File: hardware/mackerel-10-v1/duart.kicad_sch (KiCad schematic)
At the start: 2 parts, among them U6 XR68C681, X2 3.6864 MHz

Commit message: Trying to figure out Mackerel-10 components
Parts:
- added J3, J7: DE9_Plug_MountingHoles, Connector_Dsub:DSUB-9_Male_Horizontal_P2.77x2.84mm_EdgePinOffset7.70mm_Housed_MountingHolesOffset9.12mm, symbol Connector:DE9_Plug_MountingHoles
- added J4, J5: Conn_01x06, Connector_PinSocket_2.54mm:PinSocket_1x06_P2.54mm_Horizontal, symbol Connector_Generic:Conn_01x06
- added JP1, JP2: Jumper_2_Open, Connector_PinHeader_2.54mm:PinHeader_1x02_P2.54mm_Vertical, symbol Jumper:Jumper_2_Open
- added U8, U9: MAX3232, Package_DIP:DIP-16_W7.62mm, symbol Interface_UART:MAX3232
- renumbered U6 to U7
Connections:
- net +5V: now also JP1.1 (A), JP2.1 (A)
- net GND: now also J4.1 (Pin_1), J5.1 (Pin_1)
- new net: J5.3 (Pin_3), JP2.2 (B)
- new net: J4.3 (Pin_3), JP1.2 (B)
- new net RXA: J4.4 (Pin_4)
- new net RXB: J5.4 (Pin_4)
- new net TXA: J4.5 (Pin_5)
- new net TXB: J5.5 (Pin_5)
- new net /RTSA: J4.2 (Pin_2)
- new net /RTSB: J5.2 (Pin_2)
- no-connect marks 2 -> 4
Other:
- note added: "UART Headers"

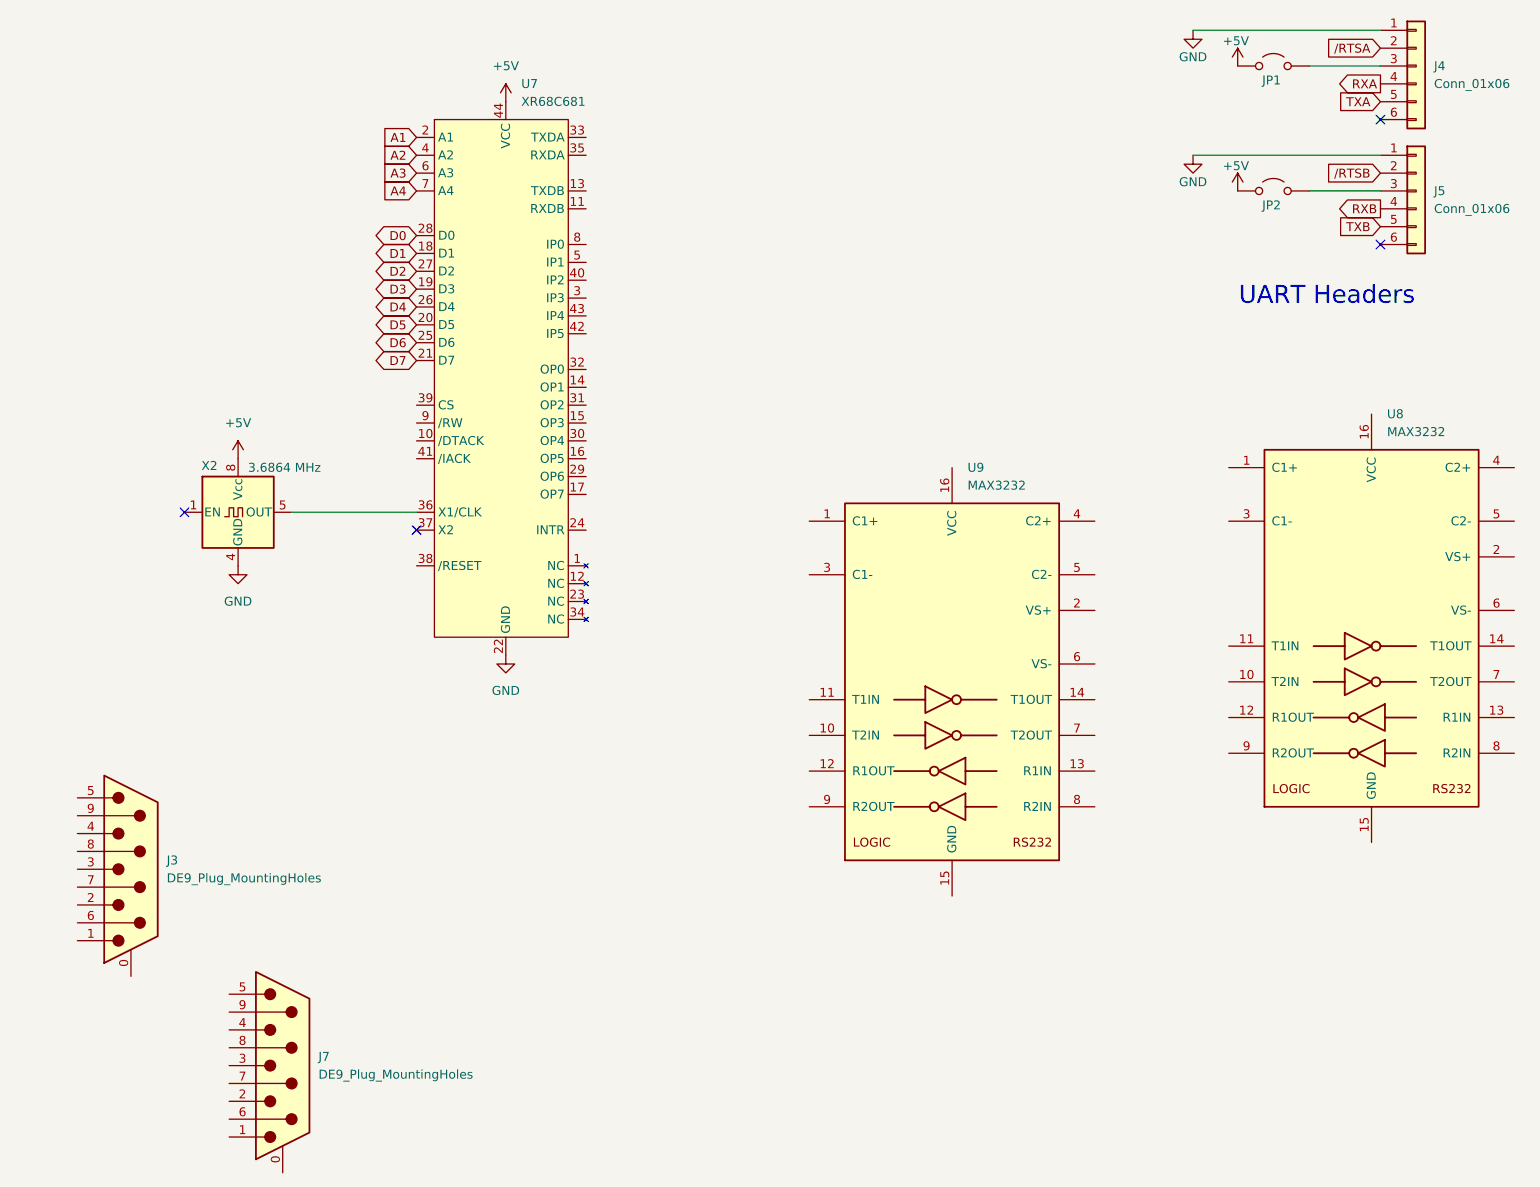
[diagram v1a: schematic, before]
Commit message: More progress on Mackerel-10 schematic and PCB
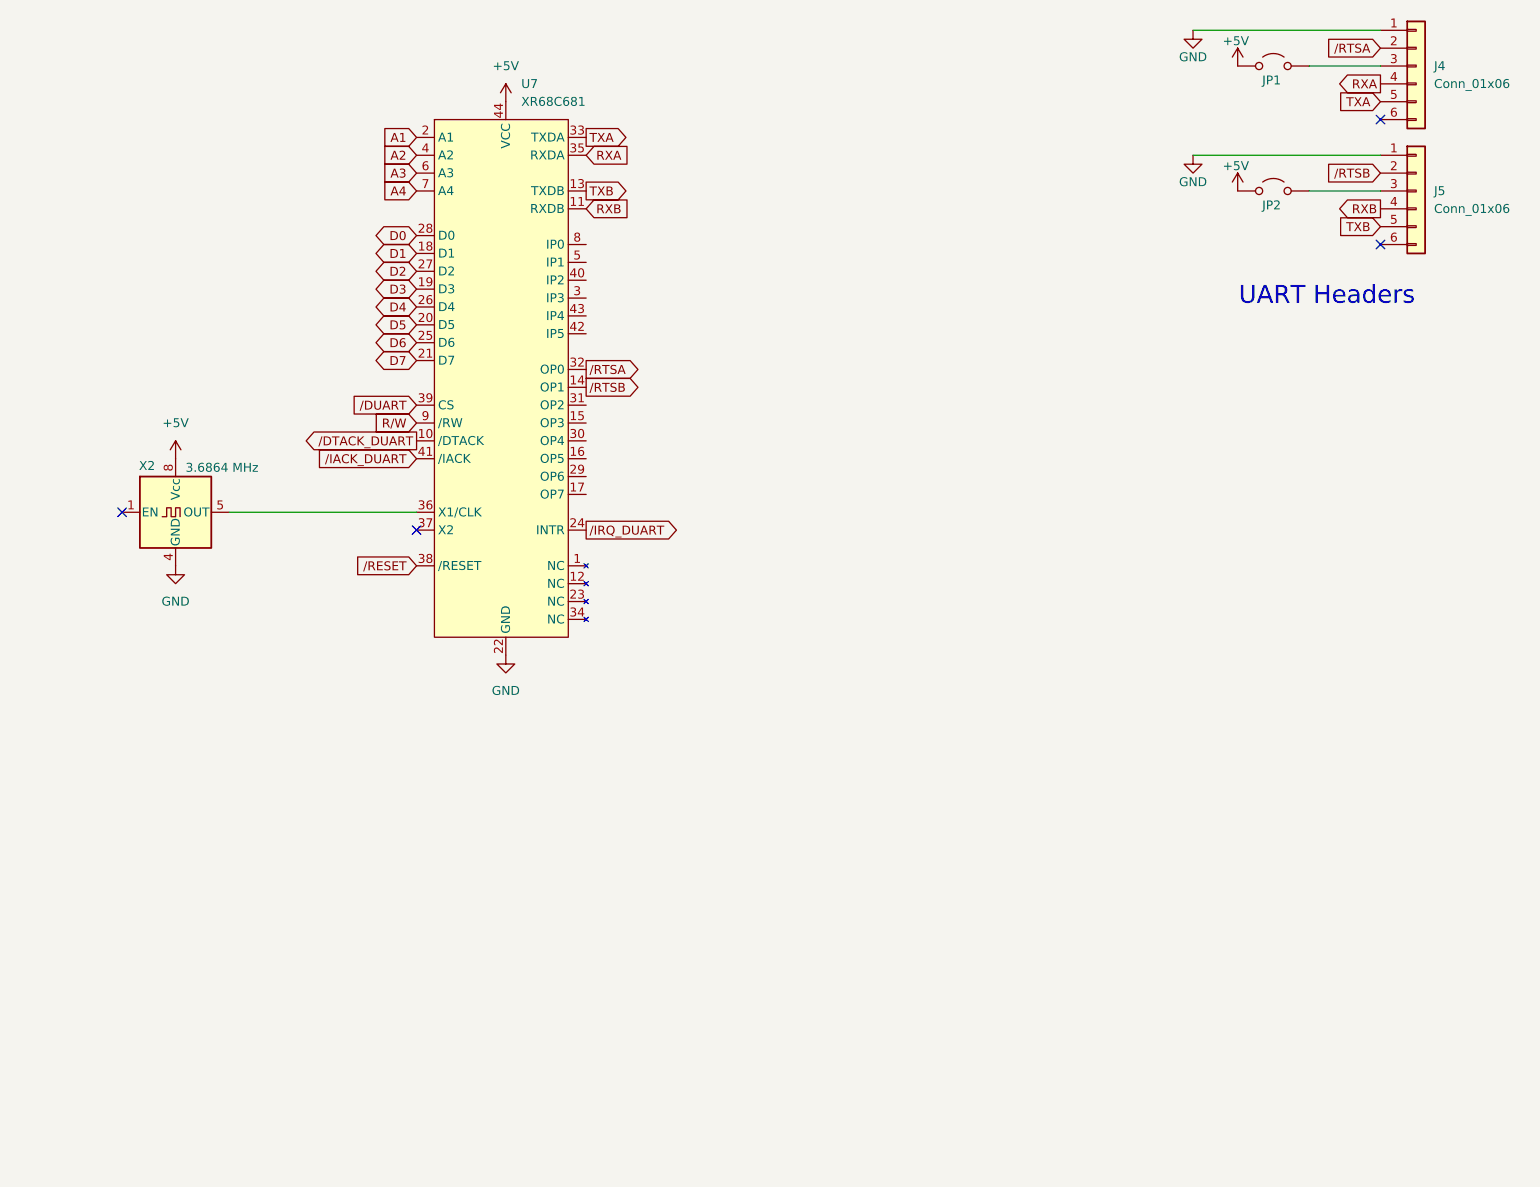
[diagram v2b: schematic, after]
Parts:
- removed J3, J7: DE9_Plug_MountingHoles, Connector_Dsub:DSUB-9_Male_Horizontal_P2.77x2.84mm_EdgePinOffset7.70mm_Housed_MountingHolesOffset9.12mm, symbol Connector:DE9_Plug_MountingHoles
- removed U8, U9: MAX3232, Package_DIP:DIP-16_W7.62mm, symbol Interface_UART:MAX3232
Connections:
- net RXA: now also U7.35 (RXDA)
- net RXB: now also U7.11 (RXDB)
- net TXA: now also U7.33 (TXDA)
- net TXB: now also U7.13 (TXDB)
- net /RTSA: now also U7.32 (OP0)
- net /RTSB: now also U7.14 (OP1)
- net /DTACK_DUART: now reaches U7.10 (/DTACK)
- net /IRQ_DUART: now reaches U7.24 (INTR)
- net /RESET: now reaches U7.38 (/RESET)
- net /DUART: now reaches U7.39 (CS)
- net /IACK_DUART: now reaches U7.41 (/IACK)
- net R/W: now reaches U7.9 (/RW)
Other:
- moved on the sheet: X2

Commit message: Rough layout of simplified Mack-10 prototype
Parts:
- removed JP1, JP2: Jumper_2_Open, Connector_PinHeader_2.54mm:PinHeader_1x02_P2.54mm_Vertical, symbol Jumper:Jumper_2_Open
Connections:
- no-connect marks 4 -> 6

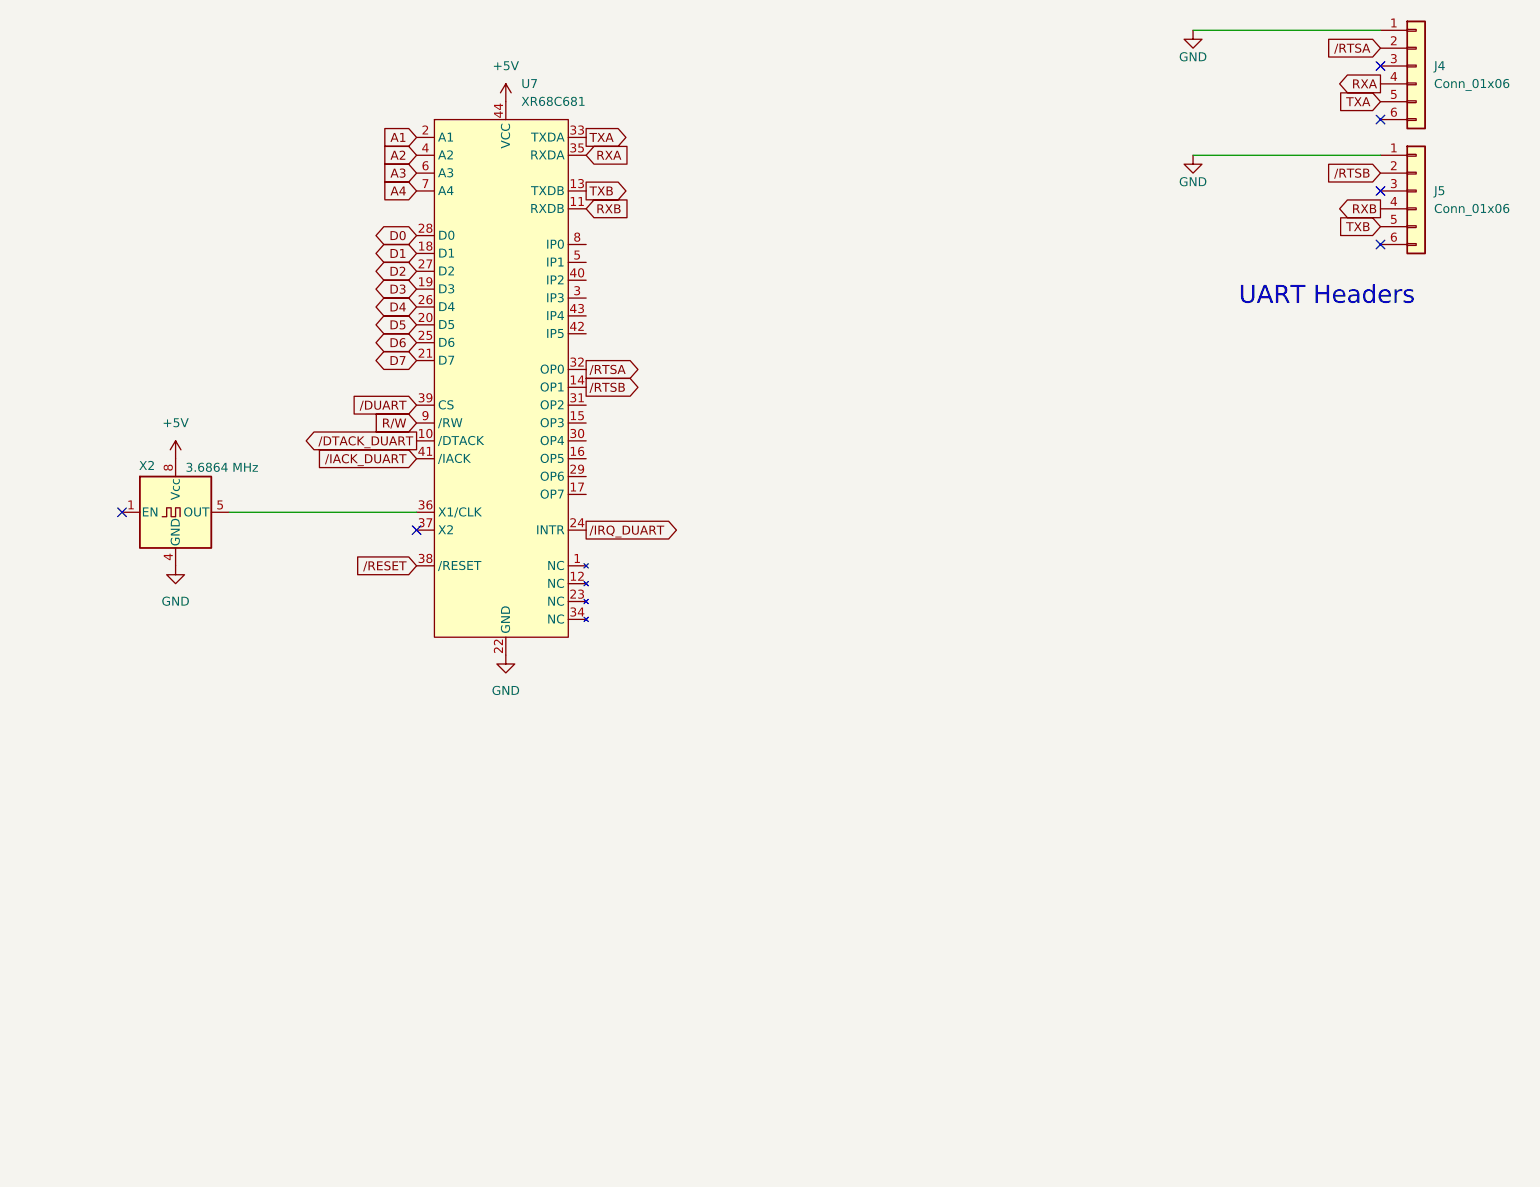
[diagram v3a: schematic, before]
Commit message: Mack-10 proto routed except for expansion headers
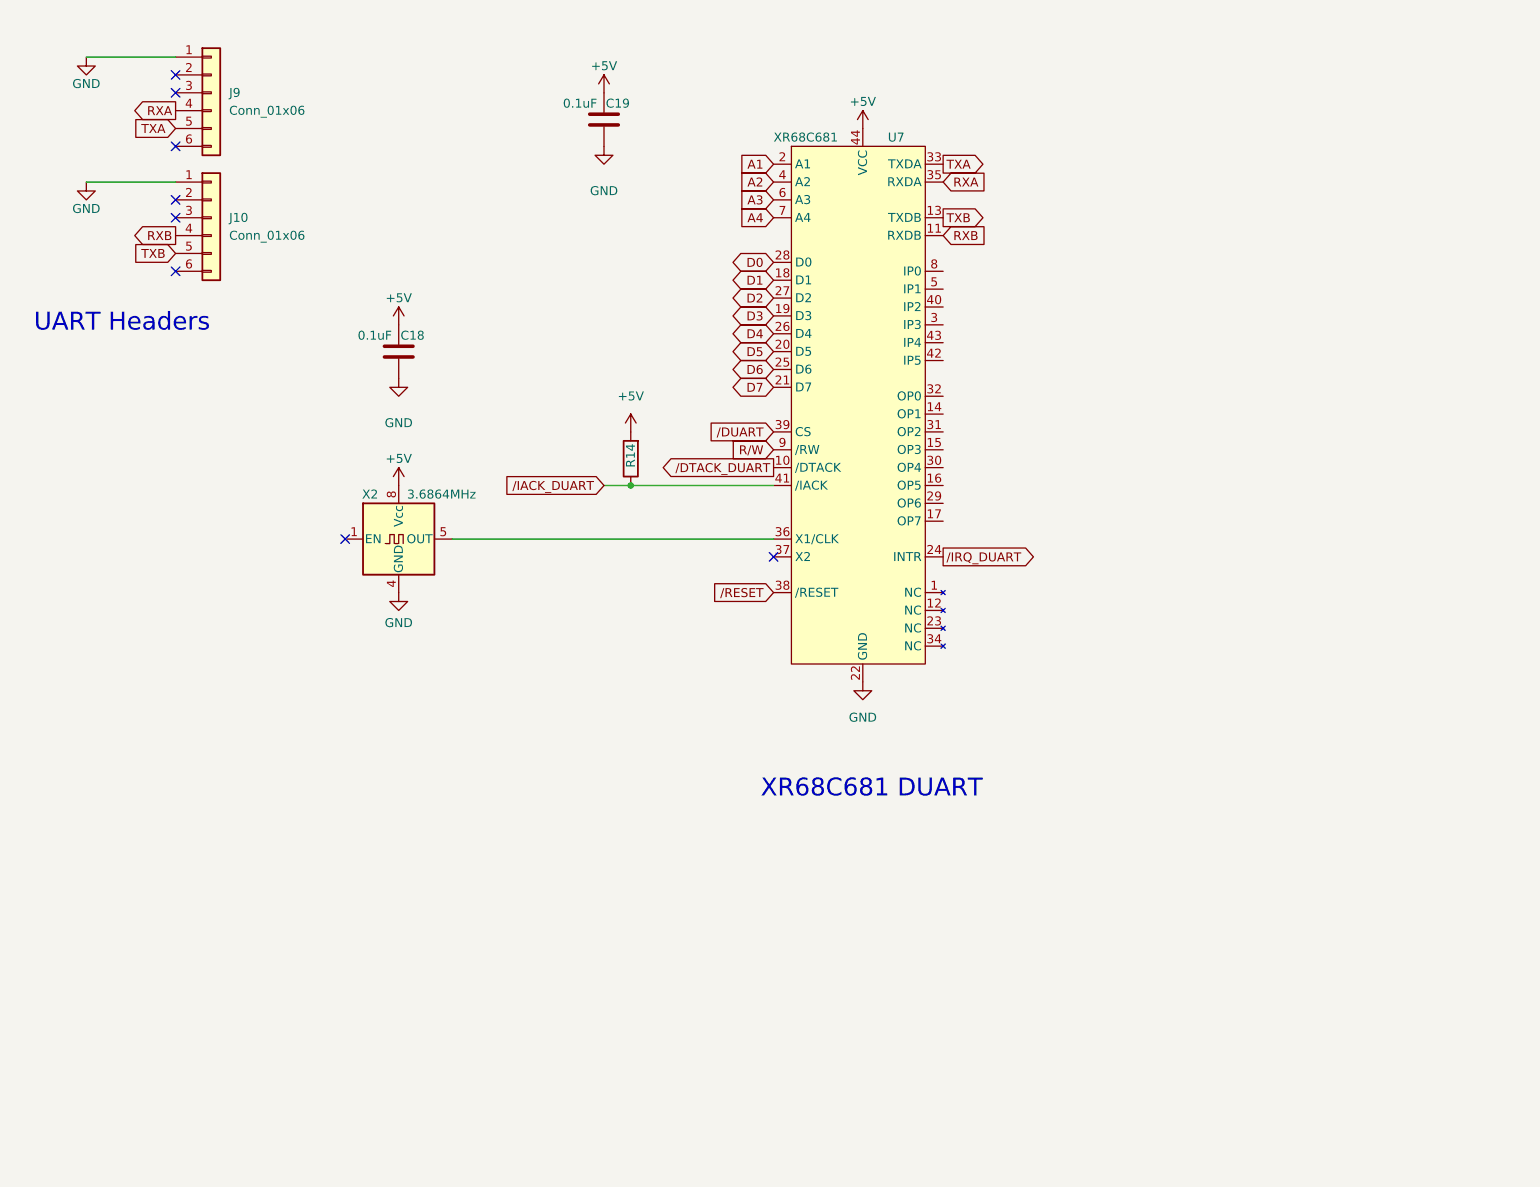
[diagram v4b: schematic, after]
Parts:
- removed J4, J5: Conn_01x06, Connector_PinSocket_2.54mm:PinSocket_1x06_P2.54mm_Horizontal, symbol Connector_Generic:Conn_01x06
- added C18, C19: 0.1uF, Capacitor_THT:C_Disc_D4.7mm_W2.5mm_P5.00mm, symbol Device:C
- added J10, J9: Conn_01x06, Connector_PinHeader_2.54mm:PinHeader_1x06_P2.54mm_Vertical, symbol Connector_Generic:Conn_01x06
- added R14: R, Resistor_THT:R_Axial_DIN0204_L3.6mm_D1.6mm_P5.08mm_Horizontal, symbol Device:R
- X2: value 3.6864 MHz -> 3.6864MHz
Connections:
- net +5V: now also C18.1, C19.1, R14.2
- net GND: now also C18.2, C19.2, J10.1 (Pin_1), J9.1 (Pin_1)
- net RXA: now also J9.4 (Pin_4)
- net RXB: now also J10.4 (Pin_4)
- net TXA: now also J9.5 (Pin_5)
- net TXB: now also J10.5 (Pin_5)
- net /IACK_DUART: now also R14.1
- net /RTSA: no longer names the net of U7.32 (OP0)
- net /RTSB: no longer names the net of U7.14 (OP1)
- no-connect marks 6 -> 8
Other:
- note added: "XR68C681 DUART"

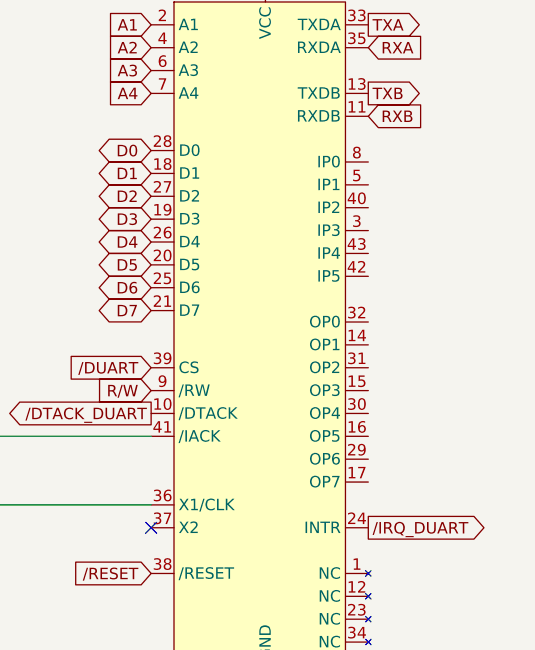
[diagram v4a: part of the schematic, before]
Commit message: Mack-10 proto routed and passing DRC
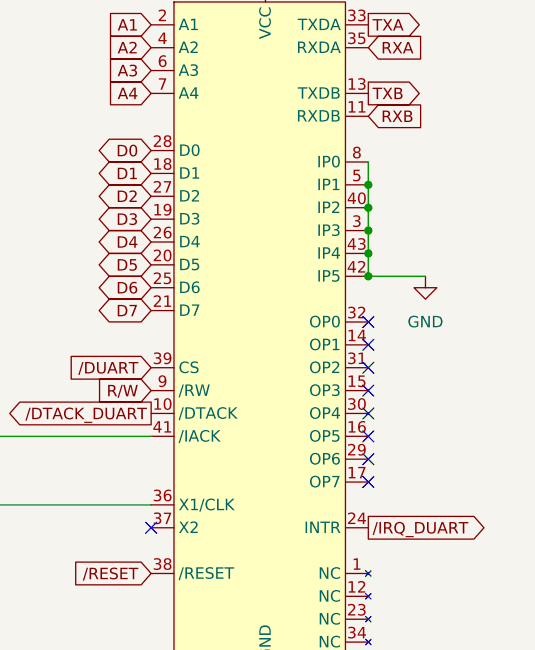
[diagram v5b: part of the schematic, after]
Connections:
- net GND: now also U7.3 (IP3), U7.40 (IP2), U7.42 (IP5), U7.43 (IP4), U7.5 (IP1), U7.8 (IP0)
- no-connect marks 8 -> 16
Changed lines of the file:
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@@
+	)
+	(junction
+		(at 166.37 66.04)
+		(diameter 0)
+		(color 0 0 0 0)
+	)
+	(junction
+		(at 166.37 76.2)
+		(diameter 0)
+		(color 0 0 0 0)
 	)
 	(junction
@@
 		(color 0 0 0 0)
 	)
+	(junction
+		(at 166.37 73.66)
+		(diameter 0)
+		(color 0 0 0 0)
+	)
+	(junction
+		(at 166.37 68.58)
+		(diameter 0)
+		(color 0 0 0 0)
+	)
+	(junction
+		(at 166.37 71.12)
+		(diameter 0)
+		(color 0 0 0 0)
+	)
+	(no_connect
+		(at 166.37 91.44)
+	)
+	(no_connect
+		(at 166.37 88.9)
+	)
 	(no_connect
 		(at 81.28 101.6)
@@
 	)
 	(no_connect
+		(at 166.37 93.98)
+	)
+	(no_connect
+		(at 166.37 86.36)
+	)
+	(no_connect
 		(at 142.24 104.14)
 	)
@@
 	)
 	(no_connect
+		(at 166.37 96.52)
+	)
+	(no_connect
 		(at 57.15 53.34)
 	)
@@
 	)
 	(no_connect
+		(at 166.37 99.06)
+	)
+	(no_connect
 		(at 57.15 38.1)
 	)
 	(no_connect
 		(at 57.15 35.56)
+	)
+	(no_connect
+		(at 166.37 83.82)
+	)
+	(no_connect
+		(at 166.37 81.28)
 	)
 	(wire
@@
 	(wire
 		(pts
-			(xy 44.45 50.8) (xy 57.15 50.8)
+			(xy 166.37 63.5) (xy 166.37 66.04)
 		)
 		(stroke
@@
 	(wire
 		(pts
-			(xy 118.11 93.98) (xy 121.92 93.98)
+			(xy 166.37 66.04) (xy 166.37 68.58)
 		)
 		(stroke
@@
 	(wire
 		(pts
+			(xy 44.45 50.8) (xy 57.15 50.8)
+		)
+		(stroke
+			(width 0)
+			(type default)
+		)
+	)
+	(wire
+		(pts
+			(xy 118.11 93.98) (xy 121.92 93.98)
+		)
+		(stroke
+			(width 0)
+			(type default)
+		)
+	)
+	(wire
+		(pts
+			(xy 166.37 73.66) (xy 166.37 76.2)
+		)
+		(stroke
+			(width 0)
+			(type default)
+		)
+	)
+	(wire
+		(pts
+			(xy 166.37 76.2) (xy 172.72 76.2)
+		)
+		(stroke
+			(width 0)
+			(type default)
+		)
+	)
+	(wire
+		(pts
 			(xy 44.45 33.02) (xy 57.15 33.02)
+		)
+		(stroke
+			(width 0)
+			(type default)
+		)
+	)
+	(wire
+		(pts
+			(xy 166.37 71.12) (xy 166.37 73.66)
+		)
+		(stroke
+			(width 0)
+			(type default)
+		)
+	)
+	(wire
+		(pts
+			(xy 166.37 68.58) (xy 166.37 71.12)
 		)
 		(stroke
@@
 					(unit 1)
 				)
+			)
+		)
+	)
+	(symbol
+		(lib_id "power:GND")
+		(at 172.72 76.2 0)
+		(unit 1)
+		(exclude_from_sim no)
+		(in_bom yes)
+		(on_board yes)
+		(dnp no)
+		(fields_autoplaced yes)
+		(property "Reference" "#PWR093"
+			(at 172.72 82.55 0)
+			(effects
+				(font
+					(size 1.27 1.27)
+				)
+				(hide yes)
+			)
+		)
+		(property "Value" "GND"
+			(at 172.72 81.28 0)
+			(effects
+				(font
+					(size 1.27 1.27)
+				)
+			)
+		)
+		(property "Footprint" ""
+			(at 172.72 76.2 0)
+			(effects
+				(font
+					(size 1.27 1.27)
+				)
+				(hide yes)
+			)
+		)
+		(property "Datasheet" ""
+			(at 172.72 76.2 0)
+			(effects
+				(font
+					(size 1.27 1.27)
+				)
+				(hide yes)
+			)
+		)
+		(property "Description" "Power symbol creates a global label with name \"GND\" , ground"
+			(at 172.72 76.2 0)
+			(effects
+				(font
+					(size 1.27 1.27)
+				)
+				(hide yes)
+			)
+		)
+		(pin "1"
+		)
+		(instances
+			(project ""
+				(path "/7c8e571b-5869-4d61-a944-e89fb22aae6e/8ac2b8a6-f372-4461-b840-cba576eacc0f"
+					(reference "#PWR093")
+					(unit 1)
+				)
